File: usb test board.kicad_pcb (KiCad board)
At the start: 2 copper layers, 37.7 x 22.6 mm, 8 parts, among them J1 Conn_01x04_Pin, J2 USB_A, J5 USB_C_Receptacle_USB2.0, J6 USB_B_Micro

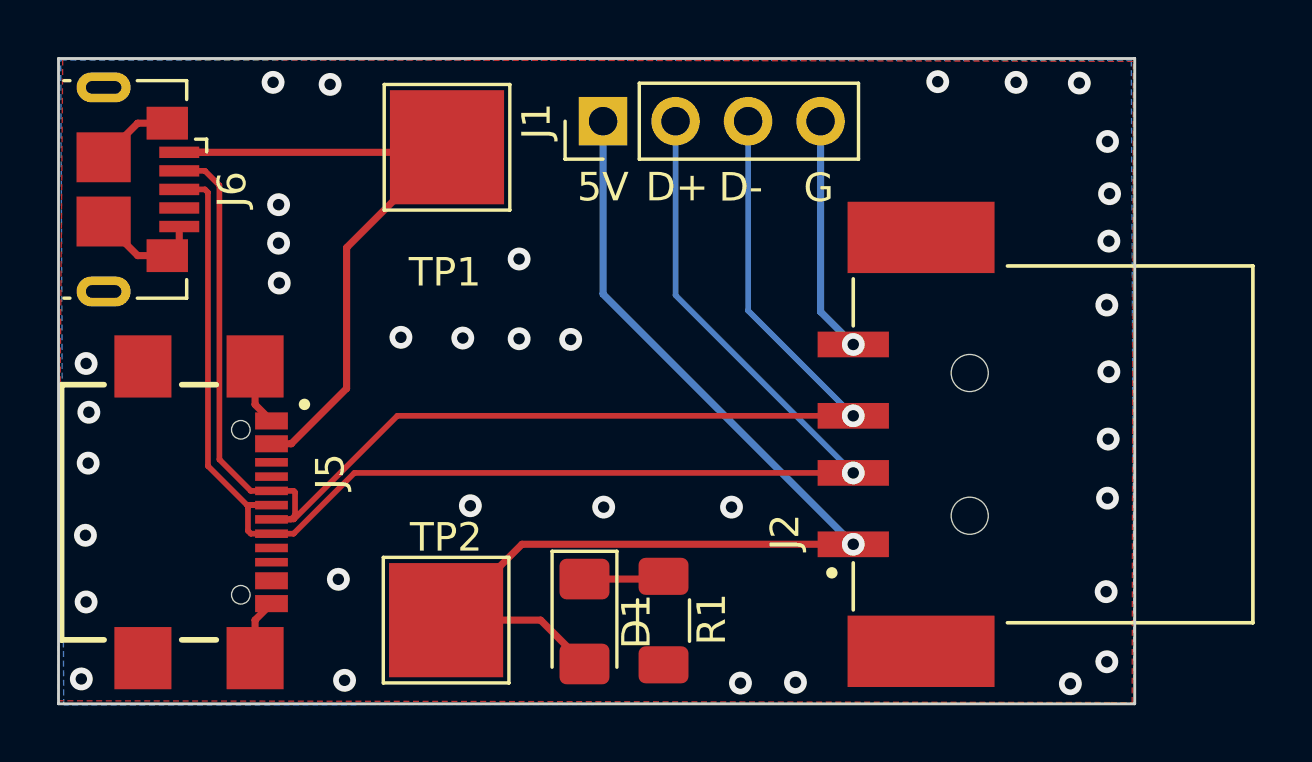
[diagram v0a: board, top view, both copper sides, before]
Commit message: Update highspeed USB differential traces
Update highspeed USB differential traces, added 0.25mm hole size microvias in the usb-c connector
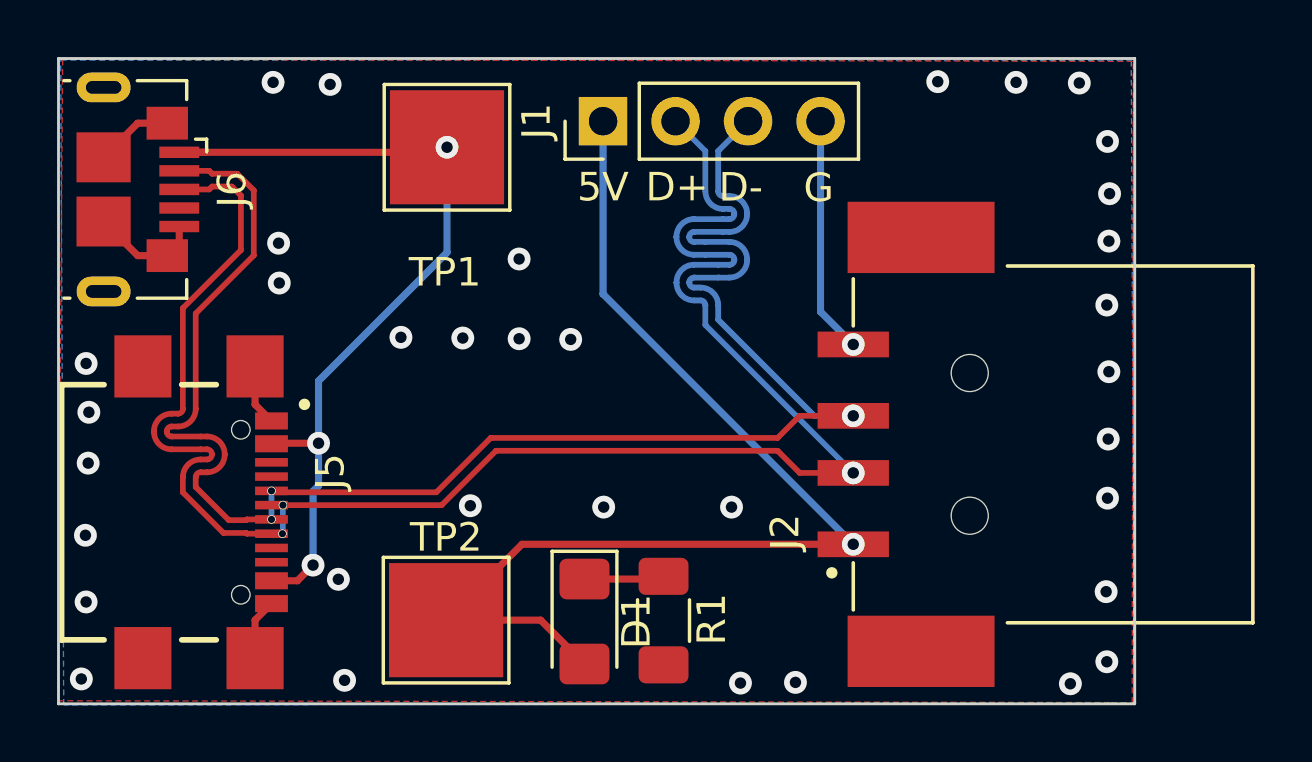
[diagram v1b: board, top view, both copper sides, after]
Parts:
- D1: footprint LED_SMD:LED_1206_3216Metric_Pad1.42x1.75mm_HandSolder -> LED_1206_3216Metric_Pad1.42x1.75mm_HandSolder
- J1: footprint Connector_PinHeader_2.54mm:PinHeader_1x04_P2.54mm_Vertical -> PinHeader_1x04_P2.54mm_Vertical
- J2: footprint UJ2-AH-4-SMT:CUI_UJ2-AH-4-SMT -> CUI_UJ2-AH-4-SMT
- J5: footprint USB4110GFA:GCT_USB4110GFA -> GCT_USB4110GFA
- J6: footprint Connector_USB:USB_Micro-B_GCT_USB3076-30-A -> USB_Micro-B_GCT_USB3076-30-A
- R1: footprint Resistor_SMD:R_1206_3216Metric_Pad1.30x1.75mm_HandSolder -> R_1206_3216Metric_Pad1.30x1.75mm_HandSolder
- TP1, TP2: footprint TestPoint:TestPoint_Pad_4.0x4.0mm -> TestPoint_Pad_4.0x4.0mm
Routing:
- net /DN: track 49.8 -> 62.5 mm, vias 1 -> 3
- net /DP: track 52.2 -> 64.7 mm, vias 1 -> 3
- net /VCC_5V: track 23.7 -> 30.3 mm, vias 0 -> 3
- net GND: vias 37 -> 36

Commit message: correct usb-a data pin polarity
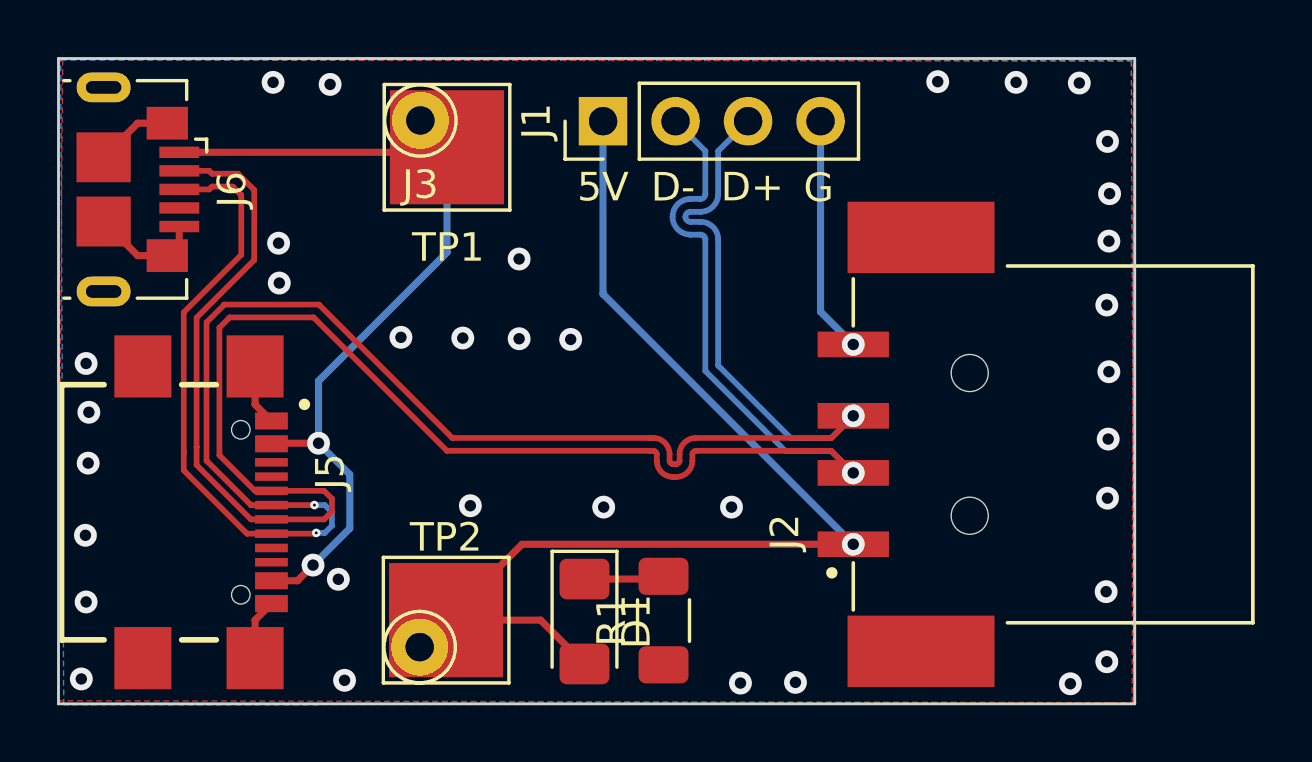
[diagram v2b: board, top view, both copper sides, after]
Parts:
- added J3: Conn_01x01_MountingPin, Connector_Pin:Pin_D1.0mm_L10.0mm, F.Cu at (98.9, 91.5)
- added J4: Conn_01x01_MountingPin, Connector_Pin:Pin_D1.0mm_L10.0mm, F.Cu at (98.9, 110.0)
- D1: footprint LED_1206_3216Metric_Pad1.42x1.75mm_HandSolder -> LED_SMD:LED_1206_3216Metric_Pad1.42x1.75mm_HandSolder
- J1: footprint PinHeader_1x04_P2.54mm_Vertical -> Connector_PinHeader_2.54mm:PinHeader_1x04_P2.54mm_Vertical
- J2: footprint CUI_UJ2-AH-4-SMT -> UJ2-AH-4-SMT:CUI_UJ2-AH-4-SMT
- J5: footprint GCT_USB4110GFA -> USB4110GFA:GCT_USB4110GFA
- J6: footprint USB_Micro-B_GCT_USB3076-30-A -> Connector_USB:USB_Micro-B_GCT_USB3076-30-A
- R1: footprint R_1206_3216Metric_Pad1.30x1.75mm_HandSolder -> Resistor_SMD:R_1206_3216Metric_Pad1.30x1.75mm_HandSolder
- TP1, TP2: footprint TestPoint_Pad_4.0x4.0mm -> TestPoint:TestPoint_Pad_4.0x4.0mm
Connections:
- J1 pad 2: /DP -> /DN
- J1 pad 3: /DN -> /DP
- J2 pad 2: /DP -> /DN
- J2 pad 3: /DN -> /DP
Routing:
- net /DN: track 62.5 -> 71.7 mm, vias 3 -> 1
- net /DP: track 64.7 -> 72.5 mm
- net /VCC_5V: track 30.3 -> 31.6 mm, vias 3 -> 2

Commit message: add revision to top silk, clean up
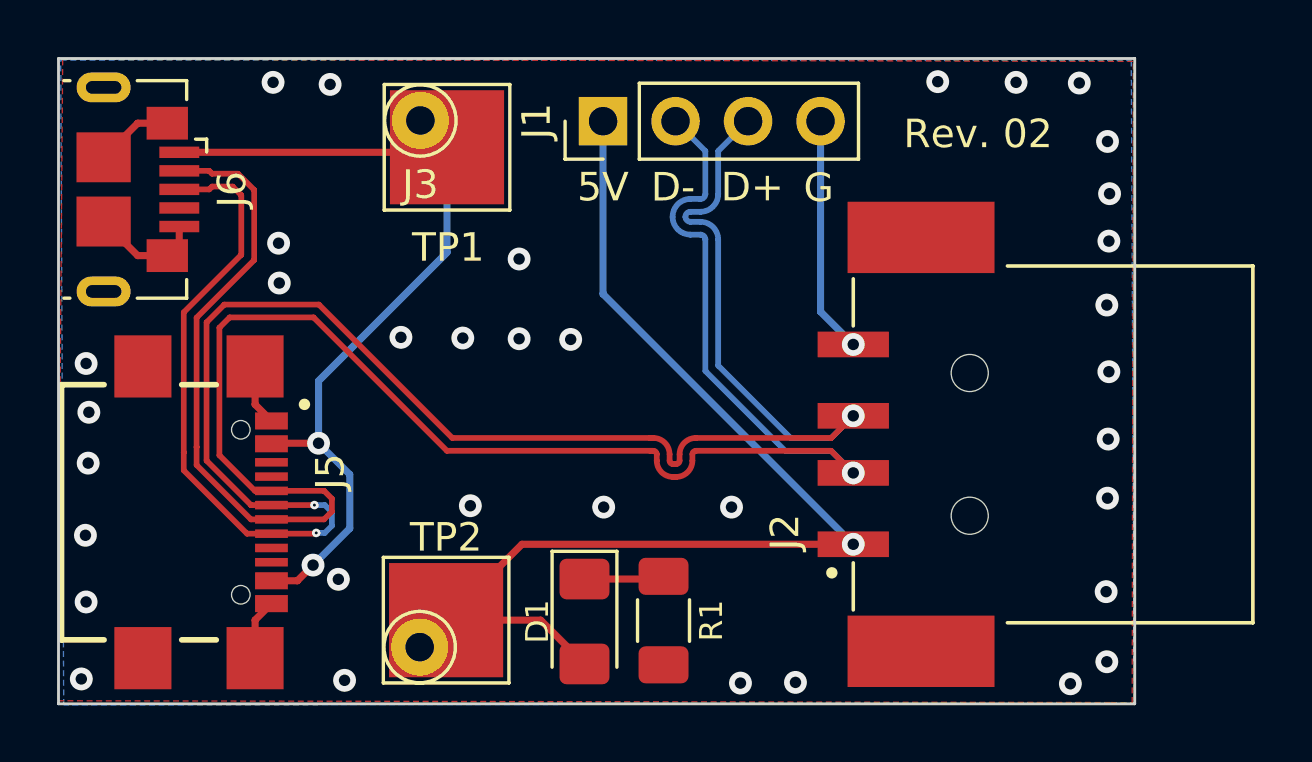
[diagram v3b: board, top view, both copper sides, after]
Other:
- board text added: "Rev. 02"
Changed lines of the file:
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@@
     (property "ki_keywords" "R res resistor")
     (attr smd)
-    (fp_text reference "R1" (at 0 -1.82 90) (layer "F.SilkS")
-        (effects (font (size 1 1) (thickness 0.15)))
+    (fp_text reference "R1" (at 0 1.675 90) (layer "F.SilkS")
+        (effects (font (size 0.8 0.8) (thickness 0.15)))
     )
     (fp_text value "R_US" (at 0 1.82 90) (layer "F.Fab")
@@
     (property "ki_keywords" "LED diode")
     (attr smd)
-    (fp_text reference "D1" (at 0 -1.82 -90) (layer "F.SilkS")
-        (effects (font (size 1 1) (thickness 0.15)))
+    (fp_text reference "D1" (at 0 1.652 -90) (layer "F.SilkS")
+        (effects (font (size 0.8 0.8) (thickness 0.15)))
     )
     (fp_text value "LED" (at 0 1.82 -90) (layer "F.Fab")
@@
     (effects (font (size 1 1) (thickness 0.15)) (justify left bottom))
   )
+  (gr_text "Rev. 02" (at 115.824 92.583) (layer "F.SilkS")
+    (effects (font (size 1 1) (thickness 0.15)) (justify left bottom))
+  )

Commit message: adjust usb connector labels
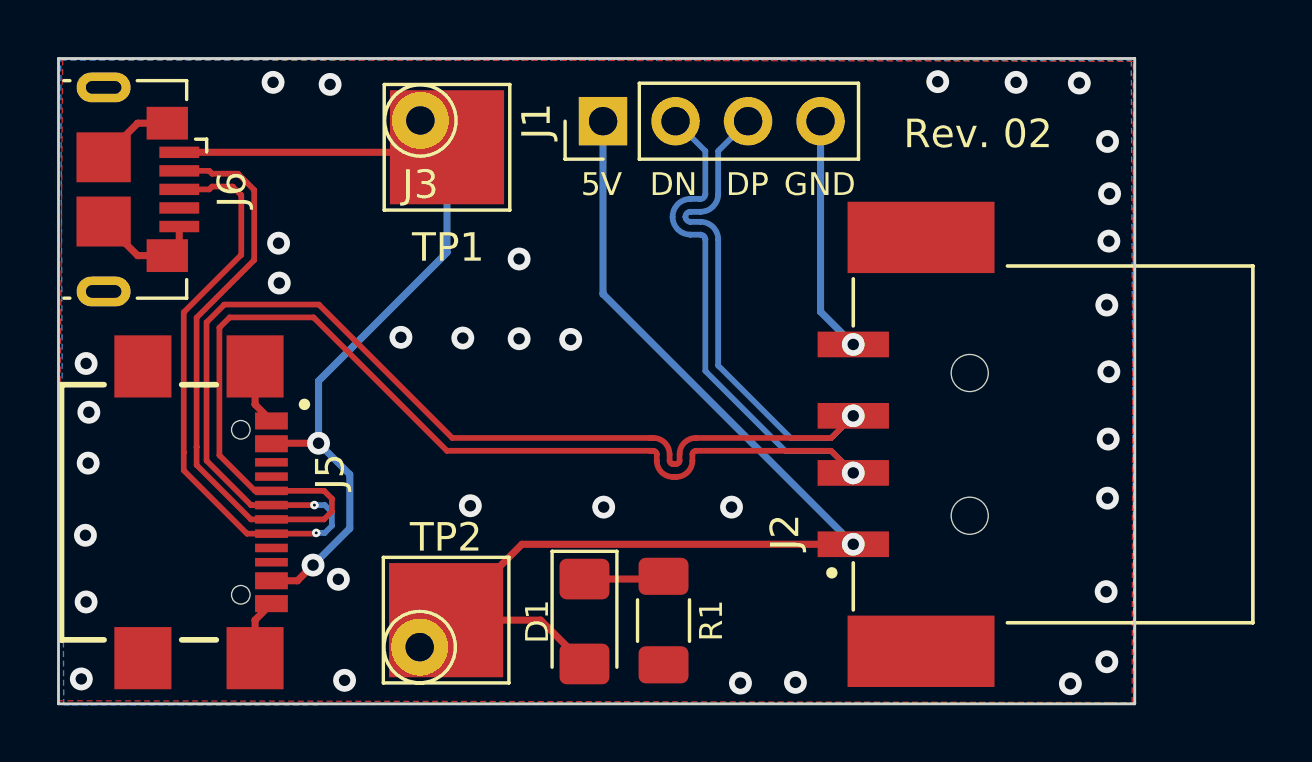
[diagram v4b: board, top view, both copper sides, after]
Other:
- board text added: "DN"
- board text added: "DP"
- board text added: "GND"
- board text removed: "D+"
- board text removed: "D-"
- board text removed: "G"
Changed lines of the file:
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@@
     (fp_line (start 1.6 0.8) (end -1.6 0.8)
       (stroke (width 0.1) (type solid)) (layer "F.Fab"))
-    (pad "1" smd roundrect (at -1.55 0 90) (size 1.3 1.75) (layers "F.Cu" "F.Paste" "F.Mask") (roundrect_rratio 0.192308)
+    (pad "1" smd roundrect (at -1.55 0 90) (size 1.3 1.75) (layers "F.Cu" "F.Paste" "F.Mask") (roundrect_rratio 0.1923076923)
       (net 4 "GND") (pintype "passive"))
-    (pad "2" smd roundrect (at 1.55 0 90) (size 1.3 1.75) (layers "F.Cu" "F.Paste" "F.Mask") (roundrect_rratio 0.192308)
+    (pad "2" smd roundrect (at 1.55 0 90) (size 1.3 1.75) (layers "F.Cu" "F.Paste" "F.Mask") (roundrect_rratio 0.1923076923)
       (net 1 "Net-(D1-K)") (pintype "passive"))
     (model "${KICAD6_3DMODEL_DIR}/Resistor_SMD.3dshapes/R_1206_3216Metric.wrl"
@@
     (fp_line (start 1.6 0.8) (end 1.6 -0.8)
       (stroke (width 0.1) (type solid)) (layer "F.Fab"))
-    (pad "1" smd roundrect (at -1.4875 0 270) (size 1.425 1.75) (layers "F.Cu" "F.Paste" "F.Mask") (roundrect_rratio 0.175439)
+    (pad "1" smd roundrect (at -1.4875 0 270) (size 1.425 1.75) (layers "F.Cu" "F.Paste" "F.Mask") (roundrect_rratio 0.1754392982)
       (net 1 "Net-(D1-K)") (pinfunction "K") (pintype "passive"))
-    (pad "2" smd roundrect (at 1.4875 0 270) (size 1.425 1.75) (layers "F.Cu" "F.Paste" "F.Mask") (roundrect_rratio 0.175439)
+    (pad "2" smd roundrect (at 1.4875 0 270) (size 1.425 1.75) (layers "F.Cu" "F.Paste" "F.Mask") (roundrect_rratio 0.1754392982)
       (net 6 "/5V") (pinfunction "A") (pintype "passive"))
     (model "${KICAD6_3DMODEL_DIR}/LED_SMD.3dshapes/LED_1206_3216Metric.wrl"
@@
   (gr_rect (start 86.222 89.355) (end 123.926 111.962)
     (stroke (width 0.1) (type default)) (fill none) (layer "Edge.Cuts"))
-  (gr_text "5V\n" (at 104.39 94.447) (layer "F.SilkS")
-    (effects (font (size 1 1) (thickness 0.15)) (justify left bottom))
+  (gr_text "5V\n" (at 104.521 94.234) (layer "F.SilkS")
+    (effects (font (size 0.8 0.8) (thickness 0.15)) (justify left bottom))
   )
   (gr_text "Rev. 02" (at 115.824 92.583) (layer "F.SilkS")
     (effects (font (size 1 1) (thickness 0.15)) (justify left bottom))
   )
-  (gr_text "G" (at 112.322 94.47) (layer "F.SilkS")
-    (effects (font (size 1 1) (thickness 0.15)) (justify left bottom))
-  )
-  (gr_text "D-" (at 106.975 94.45) (layer "F.SilkS")
-    (effects (font (size 1 1) (thickness 0.15)) (justify left bottom))
-  )
-  (gr_text "D+" (at 109.425 94.447) (layer "F.SilkS")
-    (effects (font (size 1 1) (thickness 0.15)) (justify left bottom))
+  (gr_text "GND" (at 111.633 94.234) (layer "F.SilkS")
+    (effects (font (size 0.8 0.8) (thickness 0.15)) (justify left bottom))
+  )
+  (gr_text "DN" (at 106.934 94.234) (layer "F.SilkS")
+    (effects (font (size 0.8 0.8) (thickness 0.15)) (justify left bottom))
+  )
+  (gr_text "DP" (at 109.601 94.234) (layer "F.SilkS")
+    (effects (font (size 0.8 0.8) (thickness 0.15)) (justify left bottom))
   )
   (segment (start 107.3225 107.5915) (end 107.418 107.496) (width 0.25) (layer "F.Cu") (net 1))

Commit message: Improved usb vias for easier manufacturing
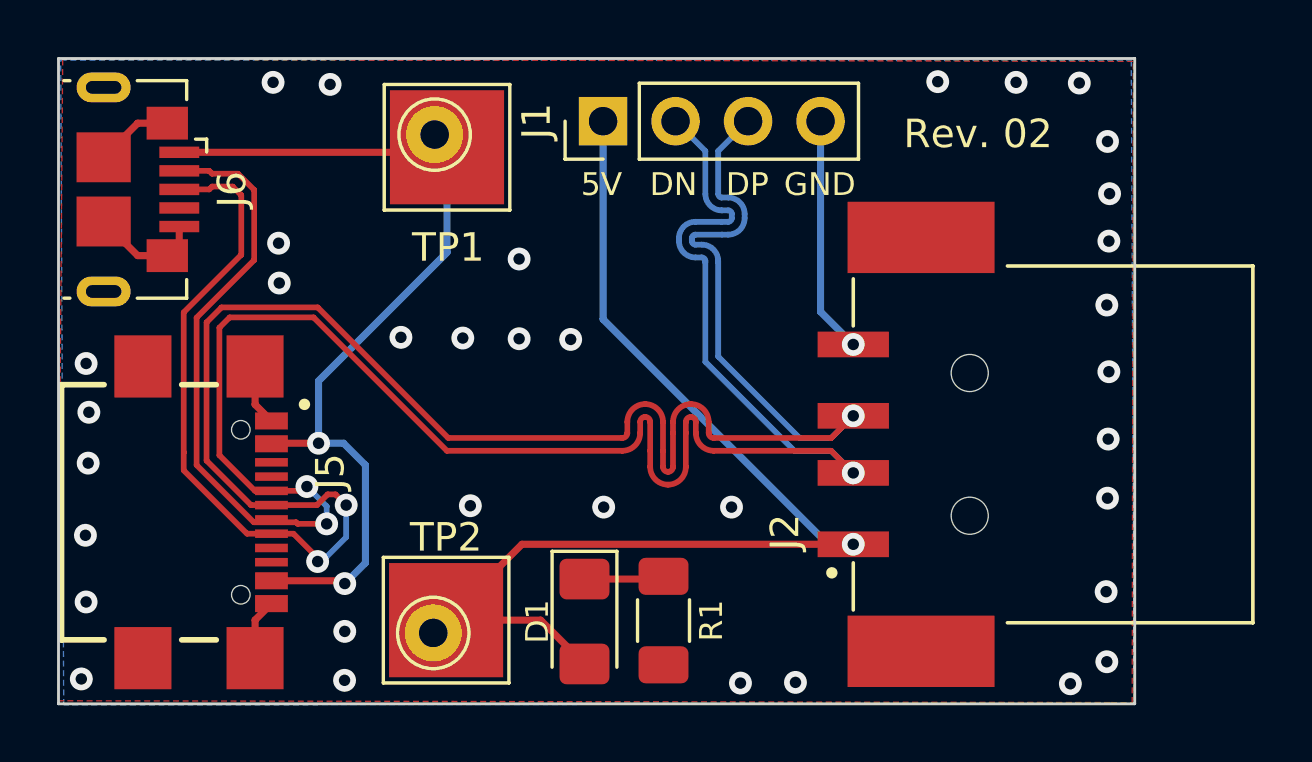
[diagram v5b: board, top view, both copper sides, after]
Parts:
- moved J3 0.70 mm to (99.4, 92.0)
- moved J4 0.69 mm to (99.3, 109.5)
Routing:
- net /DP: track 72.5 -> 80.4 mm
- net /DN: track 71.7 -> 77.2 mm, vias 1 -> 3
- net /VCC_5V: track 31.6 -> 33.7 mm
- net /5V: track 39.3 -> 39.8 mm

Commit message: improved differential pair
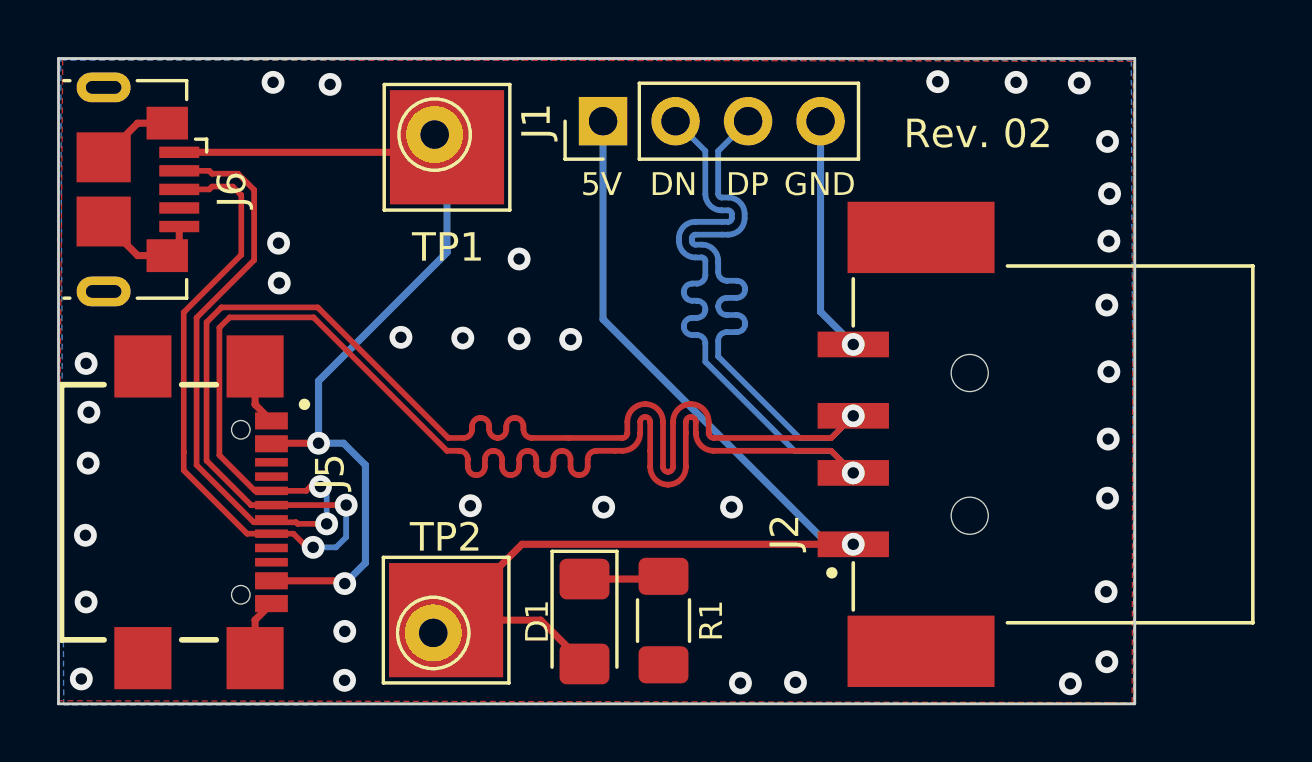
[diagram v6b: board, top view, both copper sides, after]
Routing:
- net /DN: track 77.2 -> 83.9 mm
- net /DP: track 80.4 -> 84.0 mm
